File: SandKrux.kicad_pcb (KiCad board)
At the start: 2 copper layers, 58.1 x 98.2 mm, 175 parts, among them CN2 1.25mm-2P socket, IC1 TROPIC01_chip, Q1 S8050, Q2 SI2301CDS-T1-GE3, SW1 TL3330AF130QG, SW2 TL3330AF130QG, SW3 TL3330AF130QG, SW4 TL3330AF130QG, SW5 TL3330AF130QG, U1 K210_C913414, U10 AXP173_C3345106, U11 GD32F150G8U6, U12 PCIE-67P42H, U2 MT9700, U4 XC6206P182MR_C347373, U5 GD25LQ128EWIGR, U6 TMI7003C, U7 SGM803-TXN3/TR_C5152602, U8 XC6206P302MR_C347375, U9 HX TF-CARD XG8P H1.5, X1 X322526MMB4SI, X2 X322526MMB4SI

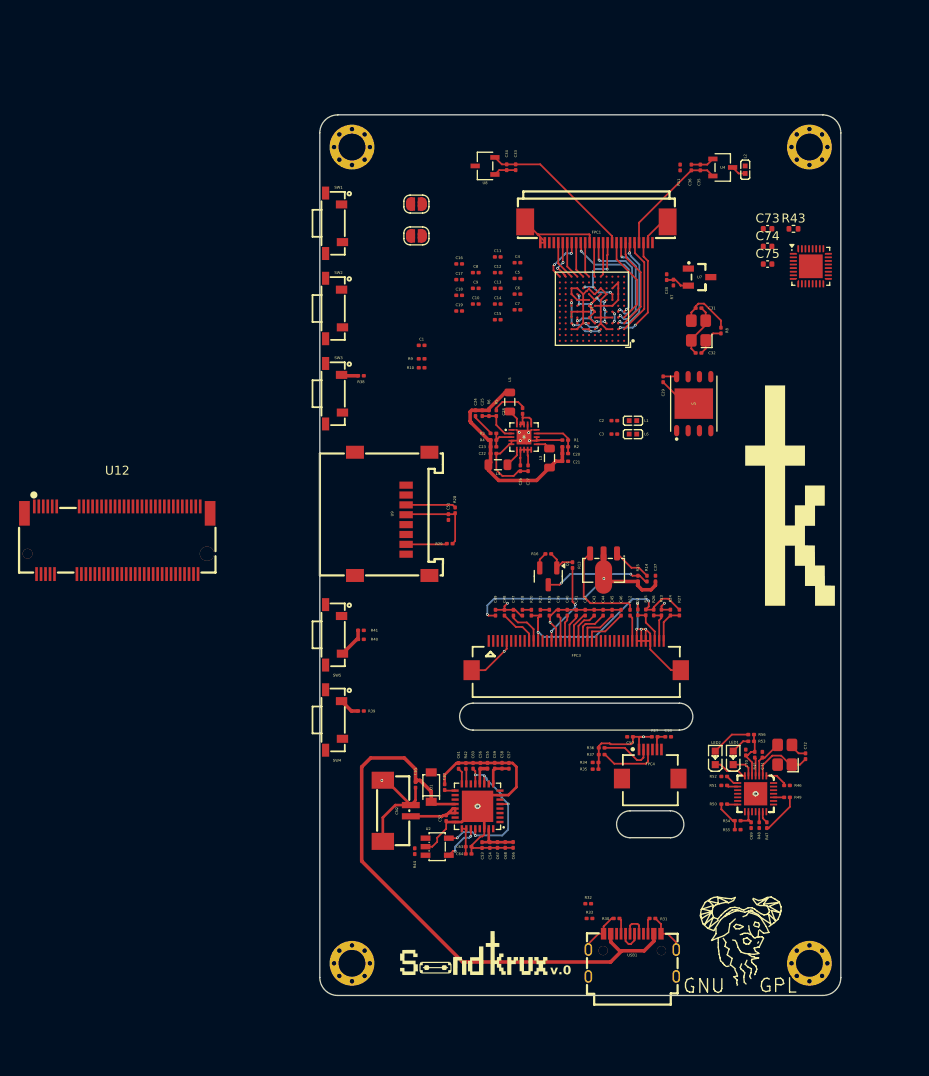
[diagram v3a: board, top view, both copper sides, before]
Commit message: posicionamento de vias e tracos entre os componentes
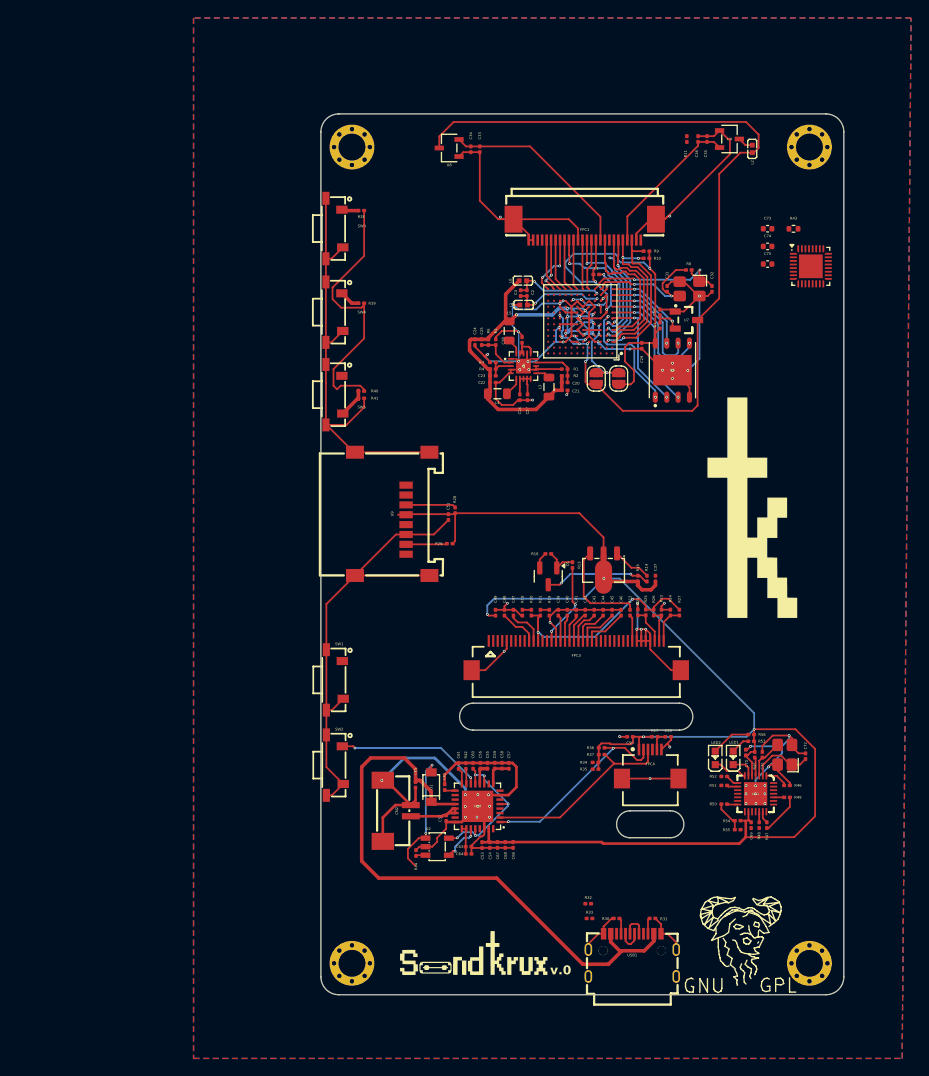
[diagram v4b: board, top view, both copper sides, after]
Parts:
- removed C10, C11, C12, C13, C14, C15, C16, C17, C8, C9: 10uF, Capacitor_SMD:C_0201_0603Metric
- removed C18, C19, C4, C5, C6, C7: 100nF, Capacitor_SMD:C_0201_0603Metric
- removed U12: PCIE-67P42H, easyeda2kicad:PCIE-SMD_75P-P0.50_HYC01B-05NGFF-420
- C31, C32: value 10pF -> 6pF
- moved SW1 50.9 mm to (81.8, 151.8)
- moved SW2 50.9 mm to (81.8, 161.3)
- moved R39 45.5 mm to (84.7, 109.8)
- moved SW4 45.5 mm to (81.7, 110.8)
- moved JP1 29.8 mm to (113.4, 118.2), turned to -90 degrees
- moved R10 27.9 mm to (116.5, 104.8)
- moved R9 27.8 mm to (116.5, 104.0)
- moved R40 27.7 mm to (84.7, 119.6)
- moved SW5 26.8 mm to (81.7, 120.0)
- moved R41 25.9 mm to (84.7, 120.4)
- moved JP2 25.6 mm to (110.9, 118.2), turned to 90 degrees
- moved L6 21.0 mm to (102.7, 107.3), turned to 180 degrees
- moved C1 21.0 mm to (110.9, 106.6)
- moved C3 18.9 mm to (102.5, 108.7), turned to 90 degrees
- moved R38 18.4 mm to (84.7, 99.5)
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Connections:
- net /k210/<NO NET> renamed +3.3V
- C2 pad 1: Net-(C2-Pad1) -> Net-(U1-VSSPLL)
- C2 pad 2: Net-(C2-Pad2) -> Net-(U1-VDDPLL)
- C3 pad 1: Net-(C2-Pad1) -> Net-(U1-VSSPLL)
- C3 pad 2: Net-(C2-Pad2) -> Net-(U1-VDDPLL)
- C31 pad 1: Net-(C31-Pad1) -> /k210/XOUT
- L1 pad 1: Net-(C2-Pad1) -> Net-(U1-VSSPLL)
- L6 pad 1: Net-(C2-Pad2) -> Net-(U1-VDDPLL)
- L6 pad 2: /k210/0v9 -> /k210/0V9
- R8 pad 1: Net-(C31-Pad1) -> /k210/XOUT
- SW1 pad 2: unconnected-(SW1-Pad2) -> GND
- SW1 pad 3: Net-(SW1-Pad3) -> GND
- SW1 pad 4: Net-(SW1-Pad3) -> GND
- U1 pad A1: /k210/LCD_RST -> /k210/IO_37
- U1 pad A2: /k210/LCD_CS -> /k210/IO_36
- U1 pad A3: /k210/IO_35 -> /k210/I2S2_SDI
- U1 pad B3: /k210/IO_34 -> /k210/I2S2_SDO
- U1 pad K4: unconnected-(U1-VSSPLL-PadK4) -> Net-(U1-VSSPLL)
- U1 pad L4: unconnected-(U1-VDDPLL-PadL4) -> Net-(U1-VDDPLL)
- X1 pad 3: Net-(C31-Pad1) -> /k210/XOUT
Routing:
- net GND: track 191.6 -> 444.4 mm, vias 18 -> 62
- net /3V3: track 57.8 -> 198.6 mm, vias 3 -> 4
- net +3.3V: track 7.96 -> 98.7 mm, vias 4 -> 5
- net /k210/1V8: track 12.5 -> 50.7 mm, vias 4 -> 5
- net /k210/0V9: track 45.3 -> 72.6 mm, vias 9 -> 10
- net /PWRON: track 0.00 -> 16.5 mm, vias 0 -> 2
- net /I2C_SDA: track 5.86 -> 21.9 mm, vias 0 -> 2
- net /I2C_SCL: track 6.64 -> 21.8 mm
- net /k210/XOUT: track 0.00 -> 15.1 mm, vias 0 -> 2
- net /k210/F_D2: track 0.00 -> 14.3 mm, vias 0 -> 2
- net /k210/F_D0: track 0.00 -> 14.0 mm, vias 0 -> 2
- net /5V: track 0.00 -> 13.9 mm, vias 0 -> 2
- net /k210/XIN: track 3.62 -> 17.4 mm, vias 0 -> 2
- net /k210/F_CS: track 0.00 -> 13.6 mm, vias 0 -> 2
- net /k210/F_D1: track 0.00 -> 13.1 mm, vias 0 -> 2
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- added copper zone on B.Cu, net GND
- added copper zone on F.Cu, net GND
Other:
- board size 58.1 x 98.2 mm -> 58.3 x 98.2 mm

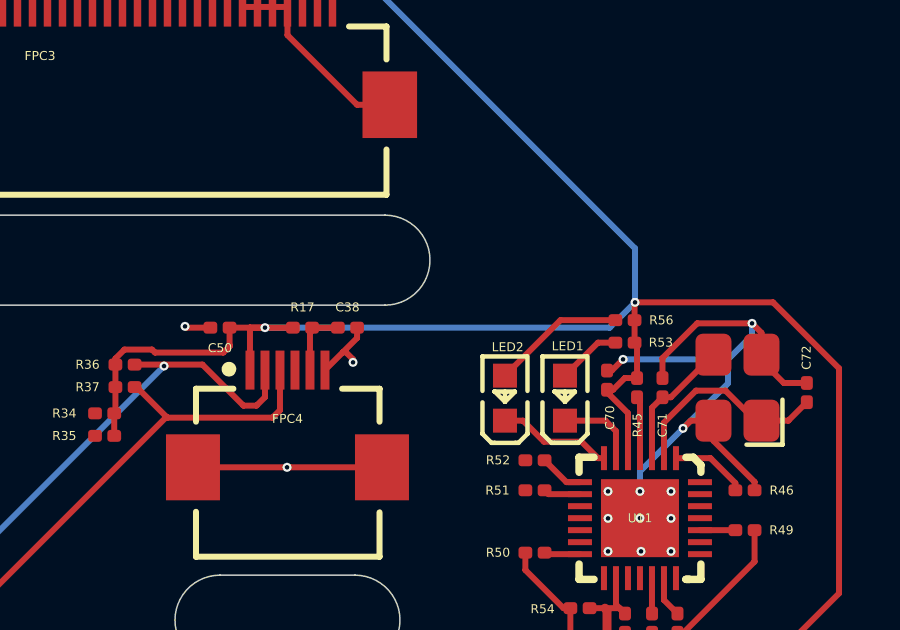
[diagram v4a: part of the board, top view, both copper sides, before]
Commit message: m2 conector diagrama na placa principal
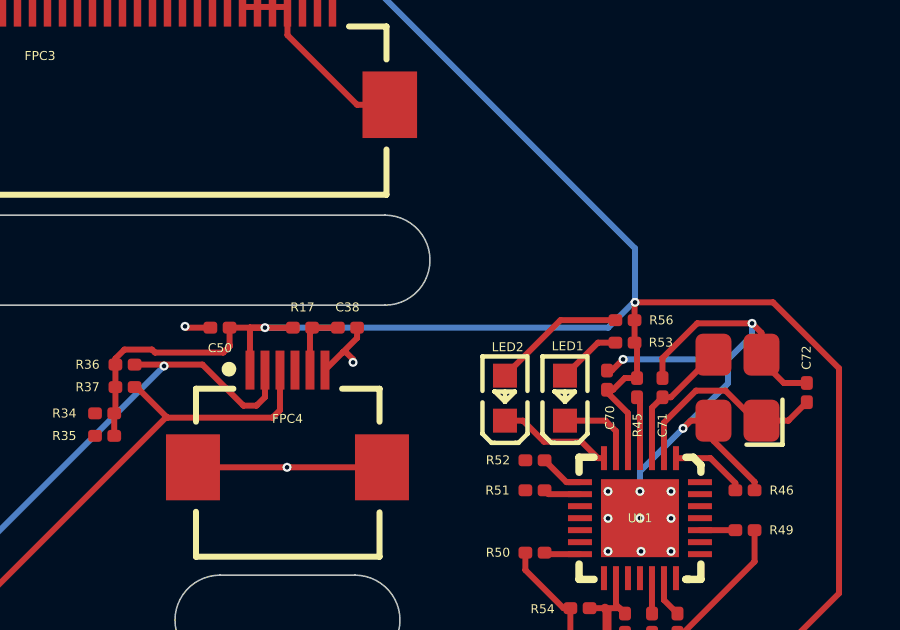
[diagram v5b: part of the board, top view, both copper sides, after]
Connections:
- net /k210/5v renamed /k210/5V
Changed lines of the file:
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@@
 	(net 131 "/k210/0V9")
 	(net 132 "/k210/Vadj")
-	(net 133 "/k210/5v")
+	(net 133 "/k210/5V")
 	(net 134 "/k210/RST")
 	(net 135 "/k210/XIN")
@@
 			(size 0.66 0.2)
 			(layers "F.Cu" "F.Mask" "F.Paste")
-			(net 133 "/k210/5v")
+			(net 133 "/k210/5V")
 			(pinfunction "VIN2")
 			(pintype "unspecified")
@@
 			(size 0.66 0.2)
 			(layers "F.Cu" "F.Mask" "F.Paste")
-			(net 133 "/k210/5v")
+			(net 133 "/k210/5V")
 			(pinfunction "EN2")
 			(pintype "unspecified")
@@
 			(size 0.66 0.2)
 			(layers "F.Cu" "F.Mask" "F.Paste")
-			(net 133 "/k210/5v")
+			(net 133 "/k210/5V")
 			(pinfunction "EN1")
 			(pintype "unspecified")
@@
 			(size 0.66 0.2)
 			(layers "F.Cu" "F.Mask" "F.Paste")
-			(net 133 "/k210/5v")
+			(net 133 "/k210/5V")
 			(pinfunction "VIN1")
 			(pintype "unspecified")
@@
 			(size 0.66 0.2)
 			(layers "F.Cu" "F.Mask" "F.Paste")
-			(net 133 "/k210/5v")
+			(net 133 "/k210/5V")
 			(pinfunction "NC")
 			(pintype "unspecified")
@@
 			(size 0.66 0.2)
 			(layers "F.Cu" "F.Mask" "F.Paste")
-			(net 133 "/k210/5v")
+			(net 133 "/k210/5V")
 			(pinfunction "EN3")
 			(pintype "unspecified")
@@
 			(size 0.66 0.2)
 			(layers "F.Cu" "F.Mask" "F.Paste")
-			(net 133 "/k210/5v")
+			(net 133 "/k210/5V")
 			(pinfunction "VIN3")
 			(pintype "unspecified")
@@
 			(layers "F.Cu" "F.Mask")
 			(roundrect_rratio 0.25)
-			(net 133 "/k210/5v")
+			(net 133 "/k210/5V")
 			(pintype "passive")
 		)
@@
 			(layers "F.Cu" "F.Mask")
 			(roundrect_rratio 0.25)
-			(net 133 "/k210/5v")
+			(net 133 "/k210/5V")
 			(pintype "passive")
 		)
@@
 			(layers "F.Cu" "F.Mask")
 			(roundrect_rratio 0.25)
-			(net 133 "/k210/5v")
+			(net 133 "/k210/5V")
 			(pintype "passive")
 		)
@@
 	)
 	(segment
-		(start 127.65625 158.14375)
-		(end 128.5 157.3)
+		(start 116.165 158.14375)
+		(end 127.60625 158.14375)
 		(width 0.2)
 		(layer "B.Cu")
@@
 	)
 	(segment
-		(start 111.745 140.505)
-		(end 109.5 142.75)
+		(start 127.60625 158.14375)
+		(end 128.45 157.3)
 		(width 0.2)
 		(layer "B.Cu")
@@
 	)
 	(segment
-		(start 116.165 158.14375)
-		(end 127.65625 158.14375)
+		(start 111.745 140.505)
+		(end 109.5 142.75)
 		(width 0.2)
 		(layer "B.Cu")
@@
 		(width 0.2)
 		(layer "B.Cu")
+		(net 138)
+	)
+	(segment
+		(start 128.45 157.3)
+		(end 128.5 157.3)
+		(width 0.2)
+		(layer "B.Cu")
